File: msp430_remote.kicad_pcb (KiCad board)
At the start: 2 copper layers, 14 parts, among them K1 CONN_3, P1 CONN_4, P2 CONN_5, P3 CONN_4X2, P4 CONN_4, U1 MSP430G2553IPW20

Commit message: done
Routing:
- net /ADC_STEER: track 22.8 -> 22.1 mm
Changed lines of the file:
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@@
     (thickness 1.6)
     (drawings 0)
-    (tracks 194)
+    (tracks 196)
     (zones 0)
     (modules 14)
@@
     )
   )
+  (segment (start 257.4 181) (end 257.835 181) (width 0.354) (layer F.Cu) (net 1))
+  (segment (start 257.835 181) (end 258.318 181.483) (width 0.354) (layer F.Cu) (net 1))
+  (segment (start 253.6 177.2) (end 257.4 181) (width 0.354) (layer F.Cu) (net 1))
   (segment (start 253.2 176.8) (end 253.2 172.8) (width 0.354) (layer F.Cu) (net 1))
-  (segment (start 258.318 180.918) (end 254.6 177.2) (width 0.354) (layer F.Cu) (net 1) (status 400000))
-  (segment (start 254.6 177.2) (end 253.6 177.2) (width 0.354) (layer F.Cu) (net 1))
   (segment (start 253.6 177.2) (end 253.2 176.8) (width 0.354) (layer F.Cu) (net 1))
-  (segment (start 258.318 181.483) (end 258.318 180.918) (width 0.354) (layer F.Cu) (net 1) (status C00000))
-  (segment (start 248.2 176.699) (end 248.666 177.165) (width 0.354) (layer F.Cu) (net 1) (status 800000))
+  (segment (start 248.2 176.699) (end 248.666 177.165) (width 0.354) (layer F.Cu) (net 1))
   (segment (start 248.2 175) (end 248.2 176.699) (width 0.354) (layer F.Cu) (net 1))
   (segment (start 250.4 172.8) (end 248.2 175) (width 0.354) (layer F.Cu) (net 1))
@@
   (segment (start 244.348 168.402) (end 243.586 169.164) (width 0.254) (layer F.Cu) (net 3))
   (segment (start 235.712 168.783) (end 234.442 168.783) (width 0.254) (layer F.Cu) (net 3))
+  (segment (start 235.2 172.72) (end 234.88 172.72) (width 0.254) (layer F.Cu) (net 4))
+  (segment (start 234.442 173.158) (end 234.442 174.117) (width 0.254) (layer F.Cu) (net 4) (status 800000))
+  (segment (start 234.88 172.72) (end 234.442 173.158) (width 0.254) (layer F.Cu) (net 4))
   (segment (start 234.442 174.117) (end 233.172 174.117) (width 0.254) (layer F.Cu) (net 4))
   (segment (start 251.968 167.767) (end 251.968 167.894) (width 0.254) (layer F.Cu) (net 4))
-  (segment (start 234.569 172.72) (end 233.172 174.117) (width 0.254) (layer F.Cu) (net 4))
-  (segment (start 247.142 172.72) (end 234.569 172.72) (width 0.254) (layer F.Cu) (net 4))
+  (segment (start 247.142 172.72) (end 235.2 172.72) (width 0.254) (layer F.Cu) (net 4))
   (segment (start 251.968 167.894) (end 247.142 172.72) (width 0.254) (layer F.Cu) (net 4))
   (segment (start 269.875 165.1) (end 265.43 165.1) (width 0.254) (layer F.Cu) (net 5))

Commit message: tentativa de por fet
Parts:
- added D1: ZENER, D3, B.Cu at (243.1, 165.5)
- added K2: CONN_3, PIN_ARRAY_3X1, F.Cu at (257.7, 163.7)
- added P5: CONN_1, PIN_ARRAY_1, F.Cu at (240.9, 178.6)
- added Q1: MOSFET_P, sot23, F.Cu at (0.00, 0.00)
- added R4: R, SM0603, F.Cu at (252.2, 165.5)
- added R5: R, SM0603, F.Cu at (249.6, 165.5)
- moved R2 2.67 mm to (244.2, 178.1)
- moved R1 2.41 mm to (246.8, 178.1)
- moved C4 0.38 mm to (233.8, 166.0)
- moved P1 0.25 mm to (254.3, 181.5), turned to 0 degrees
- moved K1 0.13 mm to (244.0, 181.6), turned to 180 degrees
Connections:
- C1 pad 1: /!RST -> /~RST
- P1 pad 2: /!RST -> /TEST
- P1 pad 3: /TEST -> /~RST
- R1 pad 1: /LED1 -> /LED2
- R2 pad 1: /LED2 -> /LED1
- R3 pad 2: /!RST -> /~RST
- U1 pad 11: /B2 -> /IRQ
- U1 pad 16: /!RST -> /~RST
- U1 pad 3: (no net) -> /pwr_pin
- U1 pad 4: (no net) -> N-0000019
- U1 pad 9: /IRQ -> /B2
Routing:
- net GND: track 104.6 -> 135.8 mm, vias 6 -> 0
- net /B2: track 8.33 -> 38.0 mm
- net /IRQ: track 30.4 -> 5.13 mm
- net /!RST: track 12.1 -> 0.00 mm
- net /~RST: track 0.00 -> 11.5 mm
- net N-0000016: track 0.00 -> 6.71 mm
- net +3.3V: track 127.7 -> 123.0 mm
- net /pwr_pin: track 0.00 -> 4.19 mm
- net /B1: track 29.0 -> 25.8 mm
- net N-000004: track 4.26 -> 2.90 mm
- net N-000002: track 4.21 -> 2.90 mm
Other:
- net class fino added: clearance 0.1, trace_width 0.254, via_dia 1.1, via_drill 0.8

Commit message: final
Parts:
- added R6: 0, SM0603, F.Cu at (240.5, 164.0)
- added R7: 0, SM0603, F.Cu at (241.8, 172.7)
- K2, P5: moved to B.Cu
- Q1: footprint sot23 -> SOT23GDS
- moved Q1 301.3 mm to (252.3, 164.6), turned to 90 degrees
- moved P5 20.4 mm to (253.7, 162.7)
- moved R4 3.05 mm to (249.2, 165.6)
- moved R5 2.61 mm to (247.7, 163.7)
- moved P4 2.54 mm to (234.4, 181.6)
- moved K2 1.53 mm to (258.8, 162.7), turned to 0 degrees
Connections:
- K2 pad 1: N-0000017 -> N-0000015
- K2 pad 2: N-0000015 -> N-0000017
- P5 pad 1: N-0000016 -> N-0000019
- R4 pad 1: N-0000015 -> N-0000017
- R4 pad 2: N-0000016 -> N-0000019
- R5 pad 1: N-0000016 -> N-0000019
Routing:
- net GND: track 135.8 -> 164.2 mm
- net N-0000017: track 0.00 -> 11.2 mm
- net N-0000019: track 0.00 -> 7.66 mm
- net N-0000016: track 6.71 -> 0.00 mm
- net +3.3V: track 123.0 -> 118.2 mm
- net N-0000015: track 0.00 -> 4.16 mm
- net /POT_STEER: track 7.89 -> 9.07 mm
- net /POT_DRIVE: track 23.2 -> 23.8 mm

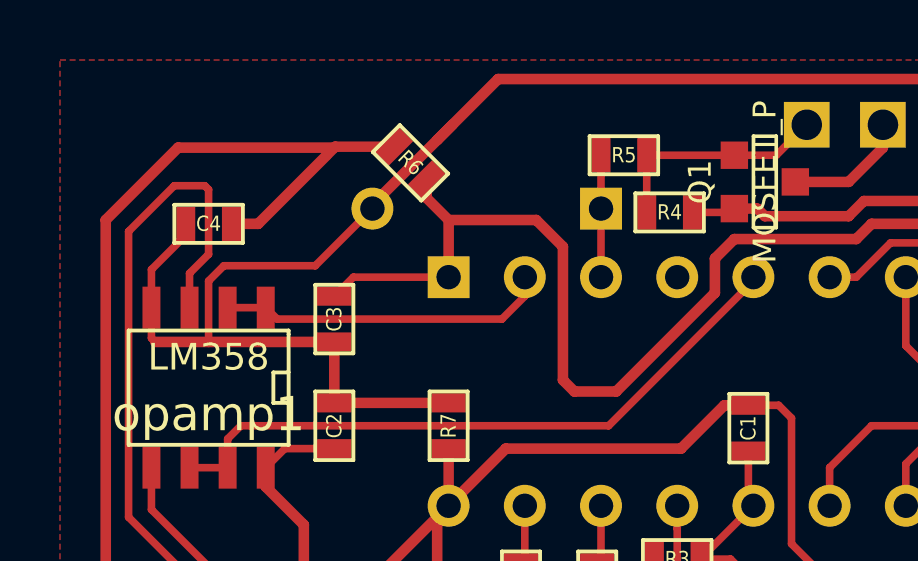
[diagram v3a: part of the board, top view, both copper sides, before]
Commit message: zener alterad
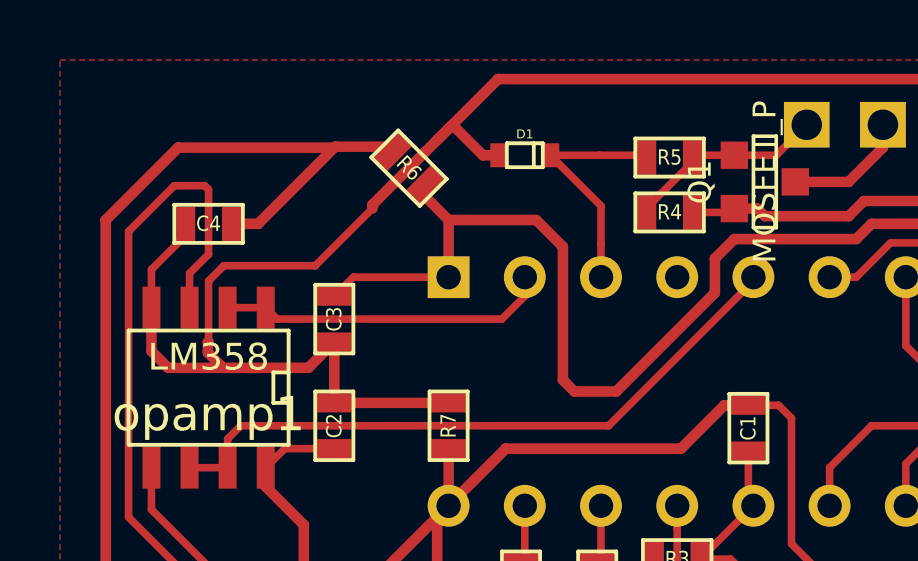
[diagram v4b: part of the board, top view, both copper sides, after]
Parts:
- D1: footprint D3 -> sod523; moved to F.Cu
- moved D1 2.18 mm to (244.3, 163.7)
- moved R5 1.53 mm to (249.2, 163.8)
- moved R6 0.18 mm to (240.5, 164.1)
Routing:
- net GND: track 164.2 -> 168.2 mm
- net /pwr_pin: track 4.06 -> 8.01 mm
- net N-0000019: track 7.66 -> 6.72 mm
